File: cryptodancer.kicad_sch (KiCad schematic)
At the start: 124 parts, among them SW1 SW_Push, SW10 SW_Push, SW11 SW_Push, SW12 SW_Push, SW13 SW_Push, SW14 SW_Push, SW15 SW_Push, SW16 SW_Push, SW17 SW_Push, SW18 SW_Push, SW19 SW_Push, SW2 SW_Push, SW20 SW_Push, SW21 SW_Push, SW22 SW_Push, SW23 SW_Push, SW24 SW_Push, SW25 SW_Push, SW26 SW_Push, SW27 SW_Push, SW28 SW_Push, SW29 SW_Push, SW3 SW_Push, SW30 SW_Push, SW31 SW_Push, SW32 SW_Push, SW33 SW_Push, SW34 SW_Push, SW35 SW_Push, SW36 SW_Push, SW37 SW_Push, SW38 SW_Push, SW39 SW_Push, SW4 SW_Push, SW40 SW_Push, SW41 SW_Push, SW42 SW_Push, SW43 SW_Push, SW44 SW_Push, SW45 SW_Push, SW46 SW_Push, SW47 SW_Push, SW48 SW_Push, SW49 SW_Push, SW5 SW_Push, SW50 SW_Push, SW51 SW_Push, SW52 SW_Push, SW53 SW_Push, SW54 SW_Push, SW55 SW_Push, SW56 SW_Push, SW57 SW_Push, SW58 SW_Push, SW59 SW_Push, SW6 SW_Push, SW60 SW_Push, SW7 SW_Push, SW8 SW_Push, SW9 SW_Push

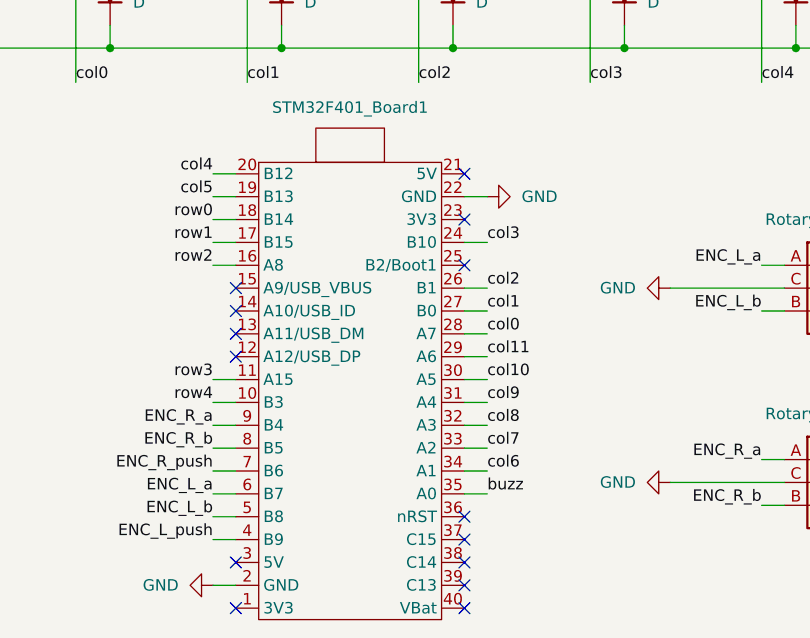
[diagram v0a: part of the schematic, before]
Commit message: use pin A4 for the buzzer
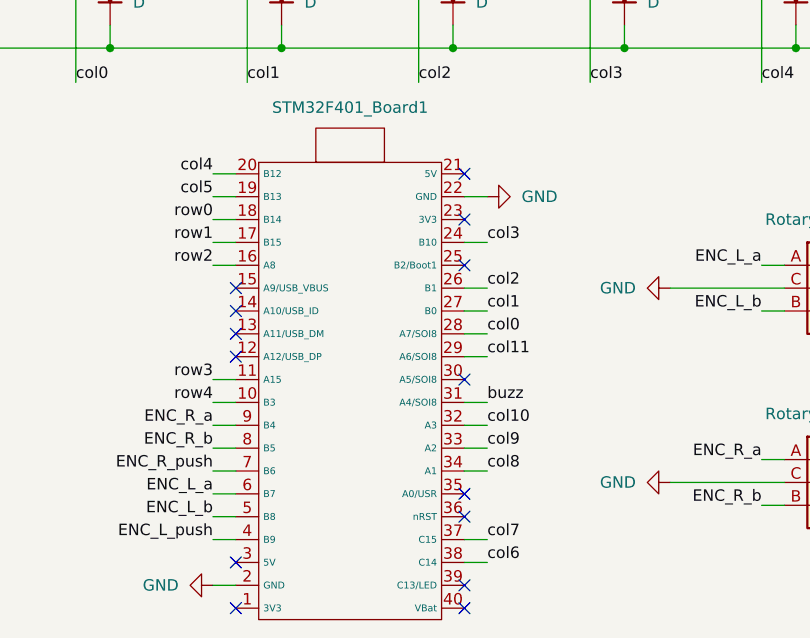
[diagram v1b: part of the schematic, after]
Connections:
- net buzz: now also STM32F401_Board1.31 (A4/SOI8); no longer STM32F401_Board1.35 (A0)
- net col10: now also STM32F401_Board1.32 (A3); no longer STM32F401_Board1.30 (A5)
- net col6: now also STM32F401_Board1.38 (C14); no longer STM32F401_Board1.34 (A1)
- net col7: now also STM32F401_Board1.37 (C15); no longer STM32F401_Board1.33 (A2)
- net col8: now also STM32F401_Board1.34 (A1); no longer STM32F401_Board1.32 (A3)
- net col9: now also STM32F401_Board1.33 (A2); no longer STM32F401_Board1.31 (A4)
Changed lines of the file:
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@@
 	)
 	(no_connect
+		(at 83.82 179.07)
+	)
+	(no_connect
 		(at 83.82 181.61)
 	)
 	(no_connect
+		(at 83.82 166.37)
+	)
+	(no_connect
 		(at 83.82 143.51)
 	)
@@
 	)
 	(no_connect
-		(at 83.82 186.69)
-	)
-	(no_connect
 		(at 58.42 191.77)
 	)
@@
 	)
 	(no_connect
-		(at 83.82 184.15)
-	)
-	(no_connect
 		(at 58.42 161.29)
 	)
@@
 	(wire
 		(pts
+			(xy 86.36 186.69) (xy 83.82 186.69)
+		)
+		(stroke
+			(width 0)
+			(type default)
+		)
+	)
+	(wire
+		(pts
 			(xy 196.85 48.26) (xy 199.39 48.26)
 		)
@@
 	(wire
 		(pts
-			(xy 83.82 179.07) (xy 86.36 179.07)
-		)
-		(stroke
-			(width 0)
-			(type default)
-		)
-	)
-	(wire
-		(pts
 			(xy 106.68 156.21) (xy 119.38 156.21)
 		)
@@
 	(wire
 		(pts
+			(xy 86.36 184.15) (xy 83.82 184.15)
+		)
+		(stroke
+			(width 0)
+			(type default)
+		)
+	)
+	(wire
+		(pts
 			(xy 273.05 93.98) (xy 275.59 93.98)
 		)
@@
 	(wire
 		(pts
-			(xy 83.82 166.37) (xy 86.36 166.37)
-		)
-		(stroke
-			(width 0)
-			(type default)
-		)
-	)
-	(wire
-		(pts
 			(xy 95.25 93.98) (xy 97.79 93.98)
 		)
@@
 		)
 	)
-	(label "col7"
-		(at 86.36 173.99 0)
-		(effects
-			(font
-				(size 1.27 1.27)
-			)
-			(justify left bottom)
-		)
-	)
 	(label "col1"
 		(at 59.69 133.35 0)
@@
 		)
 	)
-	(label "col6"
-		(at 86.36 176.53 0)
-		(effects
-			(font
-				(size 1.27 1.27)
-			)
-			(justify left bottom)
-		)
-	)
 	(label "ENC_R_a"
 		(at 116.84 175.26 180)
@@
 	)
 	(label "buzz"
-		(at 182.88 163.83 180)
+		(at 86.36 168.91 0)
 		(effects
 			(font
 				(size 1.27 1.27)
 			)
-			(justify right bottom)
+			(justify left bottom)
 		)
 	)
-	(label "col8"
-		(at 86.3544 171.45 0)
+	(label "buzz"
+		(at 182.88 163.83 180)
 		(effects
 			(font
 				(size 1.27 1.27)
 			)
-			(justify left bottom)
+			(justify right bottom)
 		)
 	)
@@
 		)
 	)
+	(label "col9"
+		(at 86.36 173.99 0)
+		(effects
+			(font
+				(size 1.27 1.27)
+			)
+			(justify left bottom)
+		)
+	)
 	(label "col6"
 		(at 180.34 133.35 0)
@@
 		)
 	)
-	(label "col9"
-		(at 86.36 168.91 0)
-		(effects
-			(font
-				(size 1.27 1.27)
-			)
-			(justify left bottom)
-		)
-	)
 	(label "row0"
 		(at 279.4 38.1 0)
@@
 		)
 	)
-	(label "col10"
-		(at 86.36 166.37 0)
-		(effects
-			(font
-				(size 1.27 1.27)
-			)
-			(justify left bottom)
-		)
-	)
 	(label "ENC_L_b"
 		(at 116.84 158.75 180)
@@
 		)
 	)
-	(label "ENC_L_b"
-		(at 55.88 181.61 180)
+	(label "col6"
+		(at 86.36 186.69 0)
 		(effects
 			(font
 				(size 1.27 1.27)
 			)
-			(justify right bottom)
+			(justify left bottom)
 		)
 	)
-	(label "buzz"
-		(at 86.36 179.07 0)
+	(label "ENC_L_b"
+		(at 55.88 181.61 180)
 		(effects
 			(font
 				(size 1.27 1.27)
 			)
-			(justify left bottom)
+			(justify right bottom)
 		)
 	)
@@
 		)
 	)
+	(label "col7"
+		(at 86.36 184.15 0)
+		(effects
+			(font
+				(size 1.27 1.27)
+			)
+			(justify left bottom)
+		)
+	)
 	(label "col11"
 		(at 86.36 163.83 0)
@@
 		(effects
 			(font
+				(size 1.27 1.27)
+			)
+			(justify left bottom)
+		)
+	)
+	(label "col10"
+		(at 86.36 171.45 0)
+		(effects
+			(font
+				(size 1.27 1.27)
+			)
+			(justify left bottom)
+		)
+	)
+	(label "col8"
+		(at 86.36 176.53 0)
+		(effects
+			(font
